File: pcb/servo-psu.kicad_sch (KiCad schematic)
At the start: 0 parts

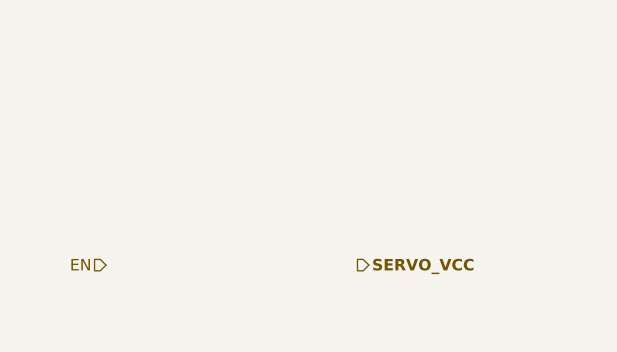
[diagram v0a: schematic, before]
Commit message: added power switch for servos
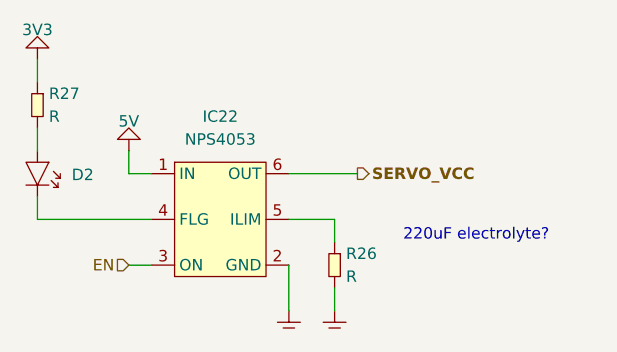
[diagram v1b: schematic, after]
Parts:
- added D2: LED, SMT:0603, symbol generic:LED
- added IC22: NPS4053, SOT:SOT-23-6, symbol Power:NPS4053
- added R26, R27: R, SMT:0603, symbol generic:R
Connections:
- net EN: now also IC22.3 (ON)
- net SERVO_VCC: now also IC22.6 (OUT)
- new net: IC22.5 (ILIM), R26.1
- new net: D2.1 (A), R27.2
- new net: D2.2 (K), IC22.4 (FLG)
- new net 3V3: R27.1
- new net GND: IC22.1 (IN), IC22.2 (GND), R26.2
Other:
- note added: "220uF electrolyte?"

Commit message: worked on layout
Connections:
- net GND: no longer IC22.1 (IN)
- new net 5V: IC22.1 (IN)
